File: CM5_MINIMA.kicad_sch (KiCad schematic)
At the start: 15 parts, among them J101 USB_C_Receptacle_USB2.0

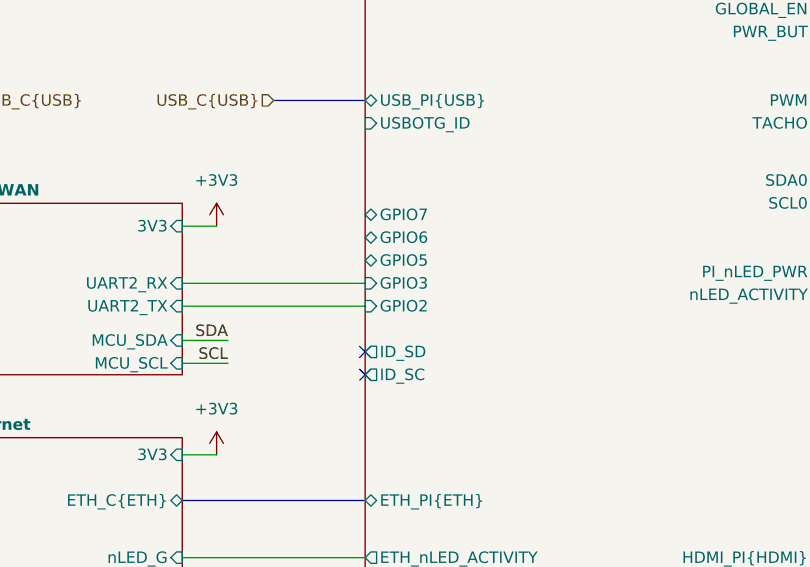
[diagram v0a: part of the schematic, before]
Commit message: RAK3172 from UART0_IR to UART3
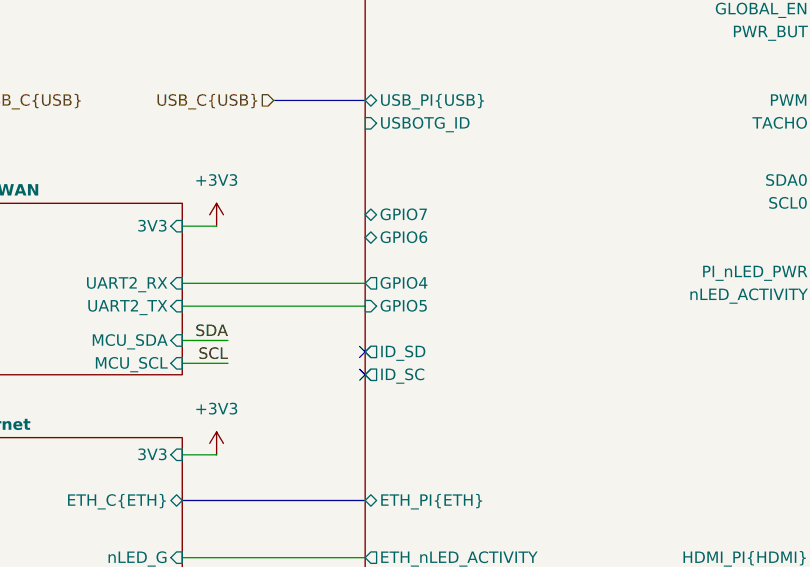
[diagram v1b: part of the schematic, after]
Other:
- sheet CM5 ports: added GPIO4; removed GPIO2, GPIO3
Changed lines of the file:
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@@
 			)
 		)
-		(pin "GPIO5" bidirectional
-			(at 130.81 97.79 180)
+		(pin "GPIO5" input
+			(at 130.81 102.87 180)
 			(effects
 				(font
@@
 			)
 		)
-		(pin "GPIO2" input
-			(at 130.81 102.87 180)
-			(effects
-				(font
-					(size 1.27 1.27)
-				)
-				(justify left)
-			)
-		)
-		(pin "GPIO3" input
-			(at 130.81 100.33 180)
-			(effects
-				(font
-					(size 1.27 1.27)
-				)
-				(justify left)
-			)
-		)
 		(pin "VBUS_EN" output
 			(at 130.81 153.67 180)
@@
 			(effects
 				(font
+					(size 1.27 1.27)
+				)
+				(justify left)
+			)
+		)
+		(pin "GPIO4" output
+			(at 130.81 100.33 180)
+			(effects
+				(font
